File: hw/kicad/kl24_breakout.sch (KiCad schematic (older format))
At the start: 64 parts, among them J1 USB-micro-ab, J2 ARM_10PIN, P1 BATT+, P10 TST, P11 TST, P12 TST, P13 TST, P14 TST, P15 TST, P16 TST, P17 TST, P18 TST, P19 TST, P2 BATT-, P20 TST, P21 TST, P22 TST, P23 TST, P24 TST, P25 TST, P26 TST, P27 TST, P28 TST, P29 TST, P3 BATT_BACKUP+, P30 TST, P31 TST, P32 TST, P33 TST, P34 TST, P35 TST, P36 TST, P4 BATT_BACKUP-, P5 TST, P6 TST, P7 TST, P8 TST, P9 TST, U1 MCP1252-33X50I, U2 MCP73831, U3 MKL24Z64VFM4, U4 MCP1640_SOT23, U5 LP3985, X1 CRYSTAL

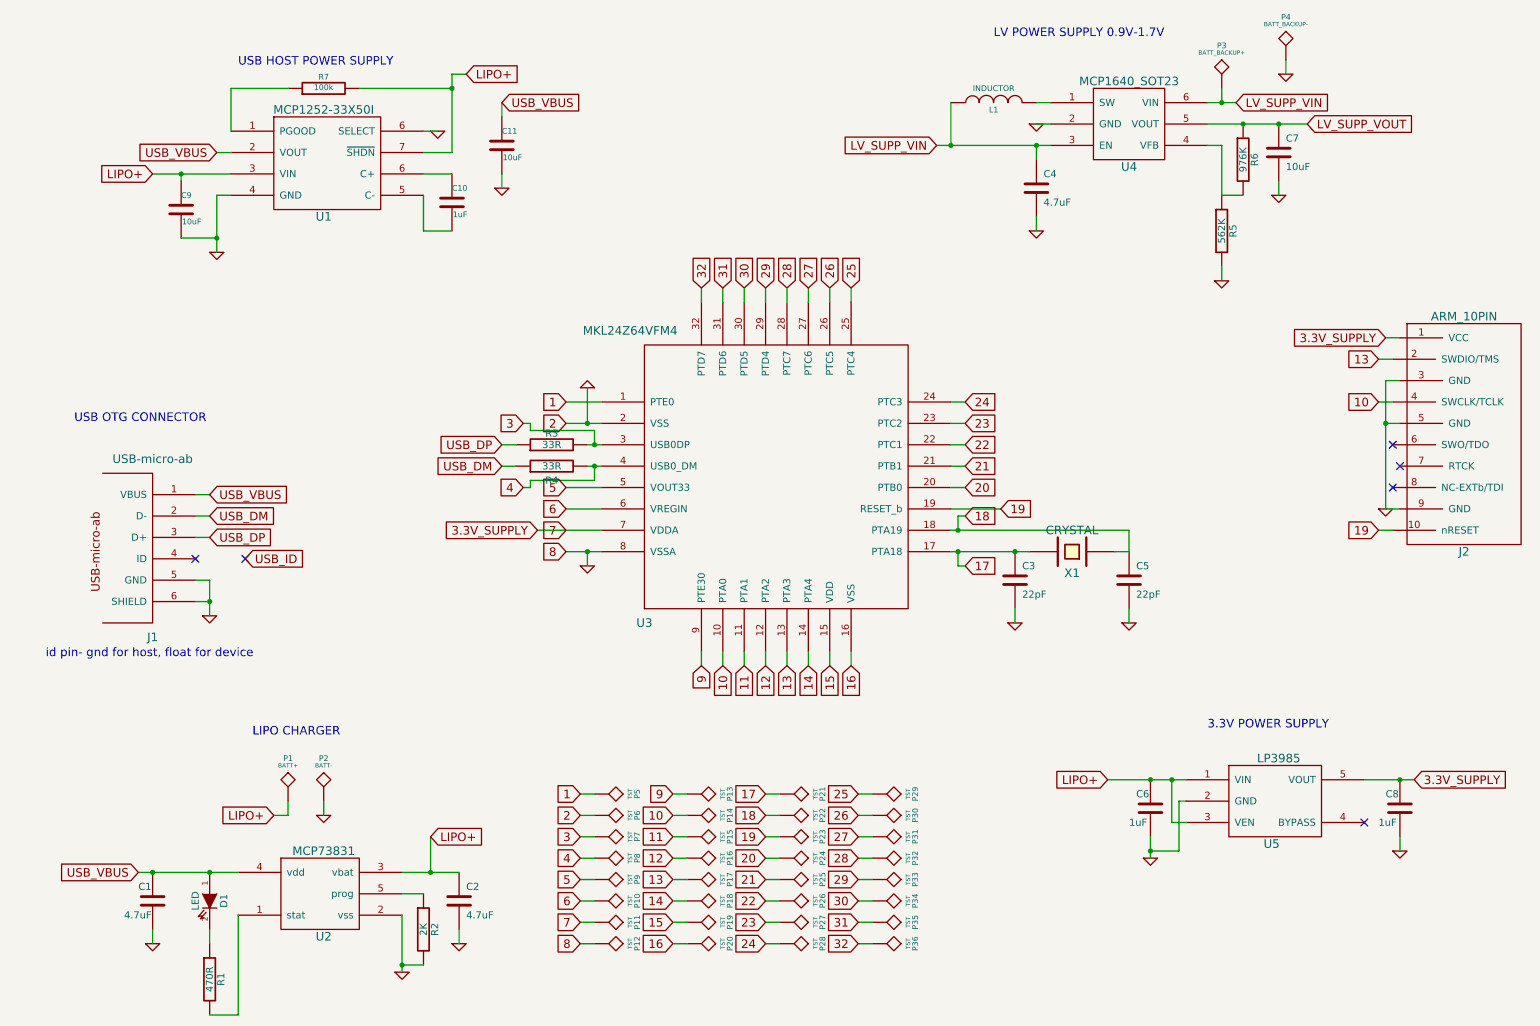
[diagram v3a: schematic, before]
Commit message: - add spi flash
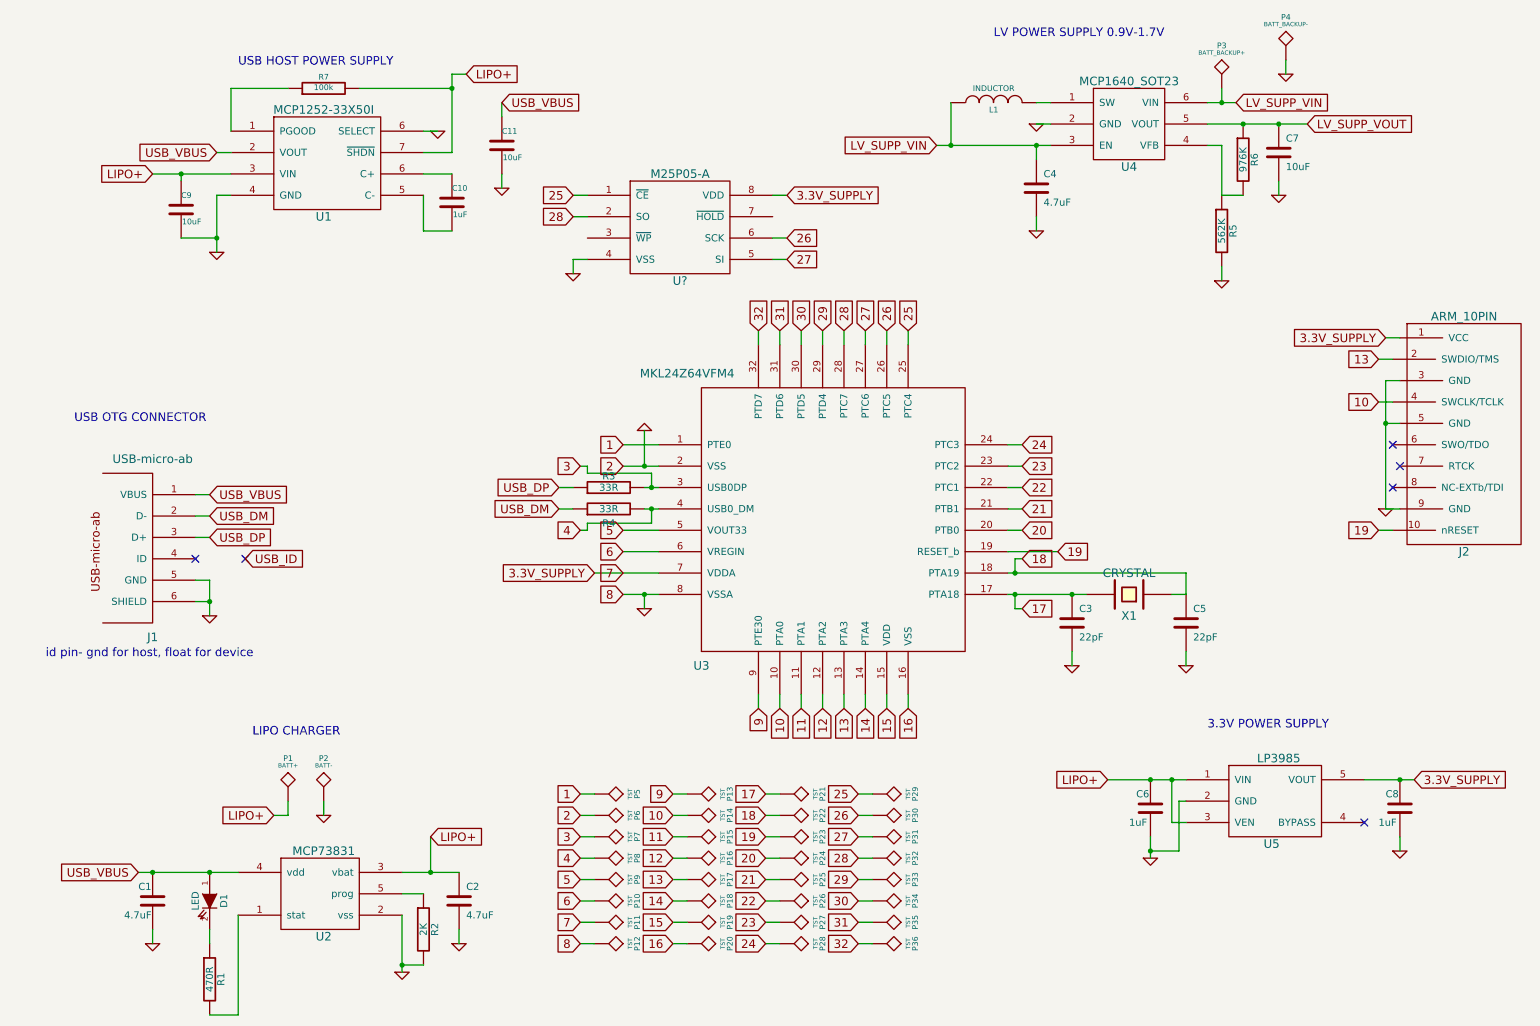
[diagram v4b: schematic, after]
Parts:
- added U?: M25P05-A, symbol M25P05-A
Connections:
- net 25: now also U?.1 (~CE)
- net 26: now also U?.6 (SCK)
- net 27: now also U?.5 (SI)
- net 28: now also U?.2 (SO)
- net 3.3V_SUPPLY: now also U?.8 (VDD)
- net GND: now also U?.4 (VSS)
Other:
- moved on the sheet: C3, C5, R3, R4, U3, X1

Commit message: - create netlist
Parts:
- gave numbers to parts that had none: 1
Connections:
- no-connect marks 6 -> 8
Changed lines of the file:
@@
-EESchema Schematic File Version 2  date 3/21/2013 8:03:57 PM
+EESchema Schematic File Version 2  date 3/21/2013 8:10:15 PM
 LIBS:power
 LIBS:device
@@
 $EndDescr
 $Comp
-L GND #PWR7
+L GND #PWR01
 U 1 1 513B71D5
 P 3500 7050
-F 0 "#PWR7" H 3500 7050 30  0001 C CNN
+F 0 "#PWR01" H 3500 7050 30  0001 C CNN
 F 1 "GND" H 3500 6980 30  0001 C CNN
 F 2 "" H 3500 7050 60  0001 C CNN
@@
 $EndComp
 $Comp
-L GND #PWR1
+L GND #PWR02
 U 1 1 513B7111
 P 1350 7050
-F 0 "#PWR1" H 1350 7050 30  0001 C CNN
+F 0 "#PWR02" H 1350 7050 30  0001 C CNN
 F 1 "GND" H 1350 6980 30  0001 C CNN
 F 2 "" H 1350 7050 60  0001 C CNN
@@
 USB_VBUS
 $Comp
-L GND #PWR5
+L GND #PWR03
 U 1 1 513B7076
 P 3100 7250
-F 0 "#PWR5" H 3100 7250 30  0001 C CNN
+F 0 "#PWR03" H 3100 7250 30  0001 C CNN
 F 1 "GND" H 3100 7180 30  0001 C CNN
 F 2 "" H 3100 7250 60  0001 C CNN
@@
 $EndComp
 $Comp
-L GND #PWR17
+L GND #PWR04
 U 1 1 513B6CEE
 P 9250 1800
-F 0 "#PWR17" H 9250 1800 30  0001 C CNN
+F 0 "#PWR04" H 9250 1800 30  0001 C CNN
 F 1 "GND" H 9250 1730 30  0001 C CNN
 F 2 "" H 9250 1800 60  0001 C CNN
@@
 $EndComp
 $Comp
-L GND #PWR16
+L GND #PWR05
 U 1 1 513B6C70
 P 8850 2400
-F 0 "#PWR16" H 8850 2400 30  0001 C CNN
+F 0 "#PWR05" H 8850 2400 30  0001 C CNN
 F 1 "GND" H 8850 2330 30  0001 C CNN
 F 2 "" H 8850 2400 60  0001 C CNN
@@
 $EndComp
 $Comp
-L GND #PWR12
+L GND #PWR06
 U 1 1 513B6C39
 P 7550 1300
-F 0 "#PWR12" H 7550 1300 30  0001 C CNN
+F 0 "#PWR06" H 7550 1300 30  0001 C CNN
 F 1 "GND" H 7550 1230 30  0001 C CNN
 F 2 "" H 7550 1300 60  0001 C CNN
@@
 $EndComp
 $Comp
-L GND #PWR13
+L GND #PWR07
 U 1 1 513B6C33
 P 7550 2050
-F 0 "#PWR13" H 7550 2050 30  0001 C CNN
+F 0 "#PWR07" H 7550 2050 30  0001 C CNN
 F 1 "GND" H 7550 1980 30  0001 C CNN
 F 2 "" H 7550 2050 60  0001 C CNN
@@
 LV_SUPP_VIN
 $Comp
-L GND #PWR2
+L GND #PWR08
 U 1 1 513B6B06
 P 1750 4750
-F 0 "#PWR2" H 1750 4750 30  0001 C CNN
+F 0 "#PWR08" H 1750 4750 30  0001 C CNN
 F 1 "GND" H 1750 4680 30  0001 C CNN
 F 2 "" H 1750 4750 60  0001 C CNN
@@
 $EndComp
 $Comp
-L GND #PWR4
+L GND #PWR09
 U 1 1 513B6AFE
 P 2550 6150
-F 0 "#PWR4" H 2550 6150 30  0001 C CNN
+F 0 "#PWR09" H 2550 6150 30  0001 C CNN
 F 1 "GND" H 2550 6080 30  0001 C CNN
 F 2 "" H 2550 6150 60  0001 C CNN
@@
 $EndComp
 $Comp
-L GND #PWR18
+L GND #PWR010
 U 1 1 513B6A86
 P 9300 950
-F 0 "#PWR18" H 9300 950 30  0001 C CNN
+F 0 "#PWR010" H 9300 950 30  0001 C CNN
 F 1 "GND" H 9300 880 30  0001 C CNN
 F 2 "" H 9300 950 60  0001 C CNN
@@
 $EndComp
 $Comp
-L GND #PWR11
+L GND #PWR011
 U 1 1 513BAD17
 P 7800 5100
-F 0 "#PWR11" H 7800 5100 30  0001 C CNN
+F 0 "#PWR011" H 7800 5100 30  0001 C CNN
 F 1 "GND" H 7800 5030 30  0001 C CNN
 F 2 "" H 7800 5100 60  0001 C CNN
@@
 $EndComp
 $Comp
-L GND #PWR14
+L GND #PWR012
 U 1 1 513BAD27
 P 8600 5100
-F 0 "#PWR14" H 8600 5100 30  0001 C CNN
+F 0 "#PWR012" H 8600 5100 30  0001 C CNN
 F 1 "GND" H 8600 5030 30  0001 C CNN
 F 2 "" H 8600 5100 60  0001 C CNN
@@
 19
 $Comp
-L GND #PWR19
+L GND #PWR013
 U 1 1 513F9714
 P 10000 4000
-F 0 "#PWR19" H 10000 4000 30  0001 C CNN
+F 0 "#PWR013" H 10000 4000 30  0001 C CNN
 F 1 "GND" H 10000 3930 30  0001 C CNN
 F 2 "" H 10000 4000 60  0001 C CNN
@@
 LIPO+
 $Comp
-L GND #PWR15
+L GND #PWR014
 U 1 1 513F9B6C
 P 8350 6450
-F 0 "#PWR15" H 8350 6450 30  0001 C CNN
+F 0 "#PWR014" H 8350 6450 30  0001 C CNN
 F 1 "GND" H 8350 6380 30  0001 C CNN
 F 2 "" H 8350 6450 60  0001 C CNN
@@
 $EndComp
 $Comp
-L GND #PWR20
+L GND #PWR015
 U 1 1 513F9C7F
 P 10100 6400
-F 0 "#PWR20" H 10100 6400 30  0001 C CNN
+F 0 "#PWR015" H 10100 6400 30  0001 C CNN
 F 1 "GND" H 10100 6330 30  0001 C CNN
 F 2 "" H 10100 6400 60  0001 C CNN
@@
 3.3V_SUPPLY
 $Comp
-L GND #PWR10
+L GND #PWR016
 U 1 1 513FA04E
 P 4800 4700
-F 0 "#PWR10" H 4800 4700 30  0001 C CNN
+F 0 "#PWR016" H 4800 4700 30  0001 C CNN
 F 1 "GND" H 4800 4630 30  0001 C CNN
 F 2 "" H 4800 4700 60  0001 C CNN
@@
 $EndComp
 $Comp
-L GND #PWR9
+L GND #PWR017
 U 1 1 513FA1BA
 P 4800 3450
-F 0 "#PWR9" H 4800 3450 30  0001 C CNN
+F 0 "#PWR017" H 4800 3450 30  0001 C CNN
 F 1 "GND" H 4800 3380 30  0001 C CNN
 F 2 "" H 4800 3450 60  0001 C CNN
@@
 3.3V_SUPPLY
 $Comp
-L GND #PWR3
+L GND #PWR018
 U 1 1 513FAD8F
 P 1800 2200
-F 0 "#PWR3" H 1800 2200 30  0001 C CNN
+F 0 "#PWR018" H 1800 2200 30  0001 C CNN
 F 1 "GND" H 1800 2130 30  0001 C CNN
 F 2 "" H 1800 2200 60  0001 C CNN
@@
 $EndComp
 $Comp
-L GND #PWR6
+L GND #PWR019
 U 1 1 514A1A73
 P 3350 1350
-F 0 "#PWR6" H 3350 1350 30  0001 C CNN
+F 0 "#PWR019" H 3350 1350 30  0001 C CNN
 F 1 "GND" H 3350 1280 30  0001 C CNN
 F 2 "" H 3350 1350 60  0001 C CNN
@@
 USB_VBUS
 $Comp
-L GND #PWR8
+L GND #PWR020
 U 1 1 514A1C2B
 P 3800 1750
-F 0 "#PWR8" H 3800 1750 30  0001 C CNN
+F 0 "#PWR020" H 3800 1750 30  0001 C CNN
 F 1 "GND" H 3800 1680 30  0001 C CNN
 F 2 "" H 3800 1750 60  0001 C CNN
@@
 NoConn ~ 2000 4350
 $Comp
-L M25P05-A U?
+L M25P05-A U6
 U 1 1 514BA0D4
 P 5050 2000
-F 0 "U?" H 5050 1600 60  0000 C CNN
+F 0 "U6" H 5050 1600 60  0000 C CNN
 F 1 "M25P05-A" H 5050 2350 60  0000 C CNN
 F 2 "" H 5100 1800 60  0000 C CNN
@@
 	4300 1800 4400 1800
 $Comp
-L GND #PWR?
+L GND #PWR021
 U 1 1 514BA584
 P 4300 2350
-F 0 "#PWR?" H 4300 2350 30  0001 C CNN
+F 0 "#PWR021" H 4300 2350 30  0001 C CNN
 F 1 "GND" H 4300 2280 30  0001 C CNN
 F 2 "" H 4300 2350 60  0001 C CNN
@@
 Wire Wire Line
 	4300 2250 4400 2250
+NoConn ~ 5700 1950
+NoConn ~ 4400 2100
 $EndSCHEMATC

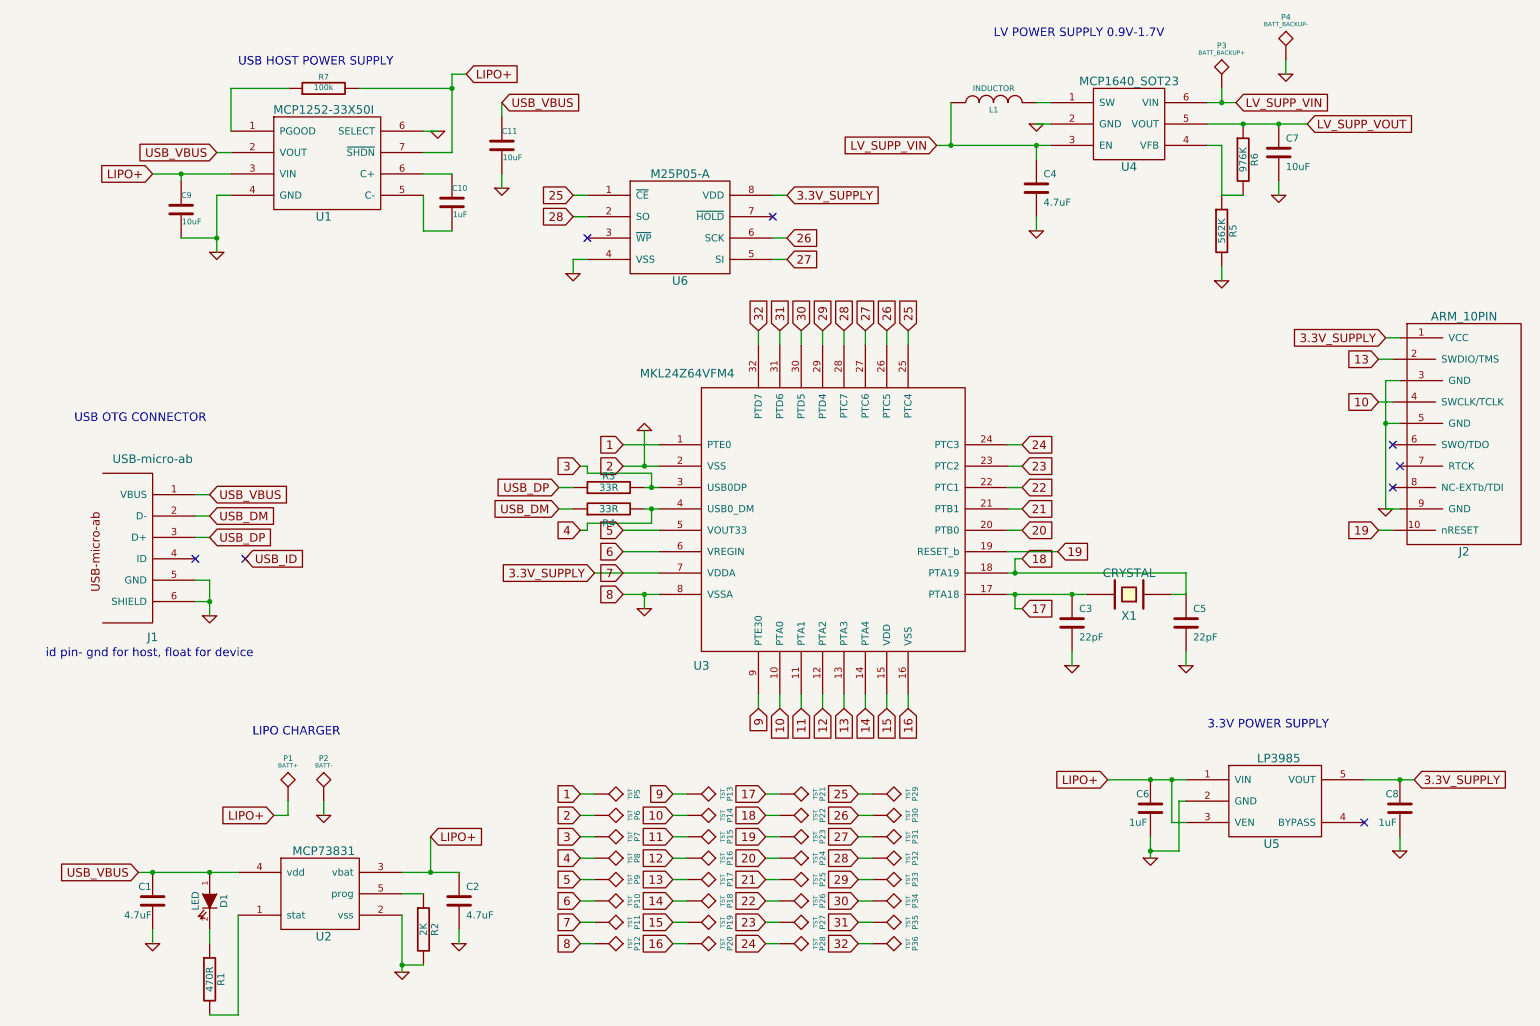
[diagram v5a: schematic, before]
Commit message: - try to rework usb host pwr supply, needs an extra switch i'm thinking, so i'm bailing
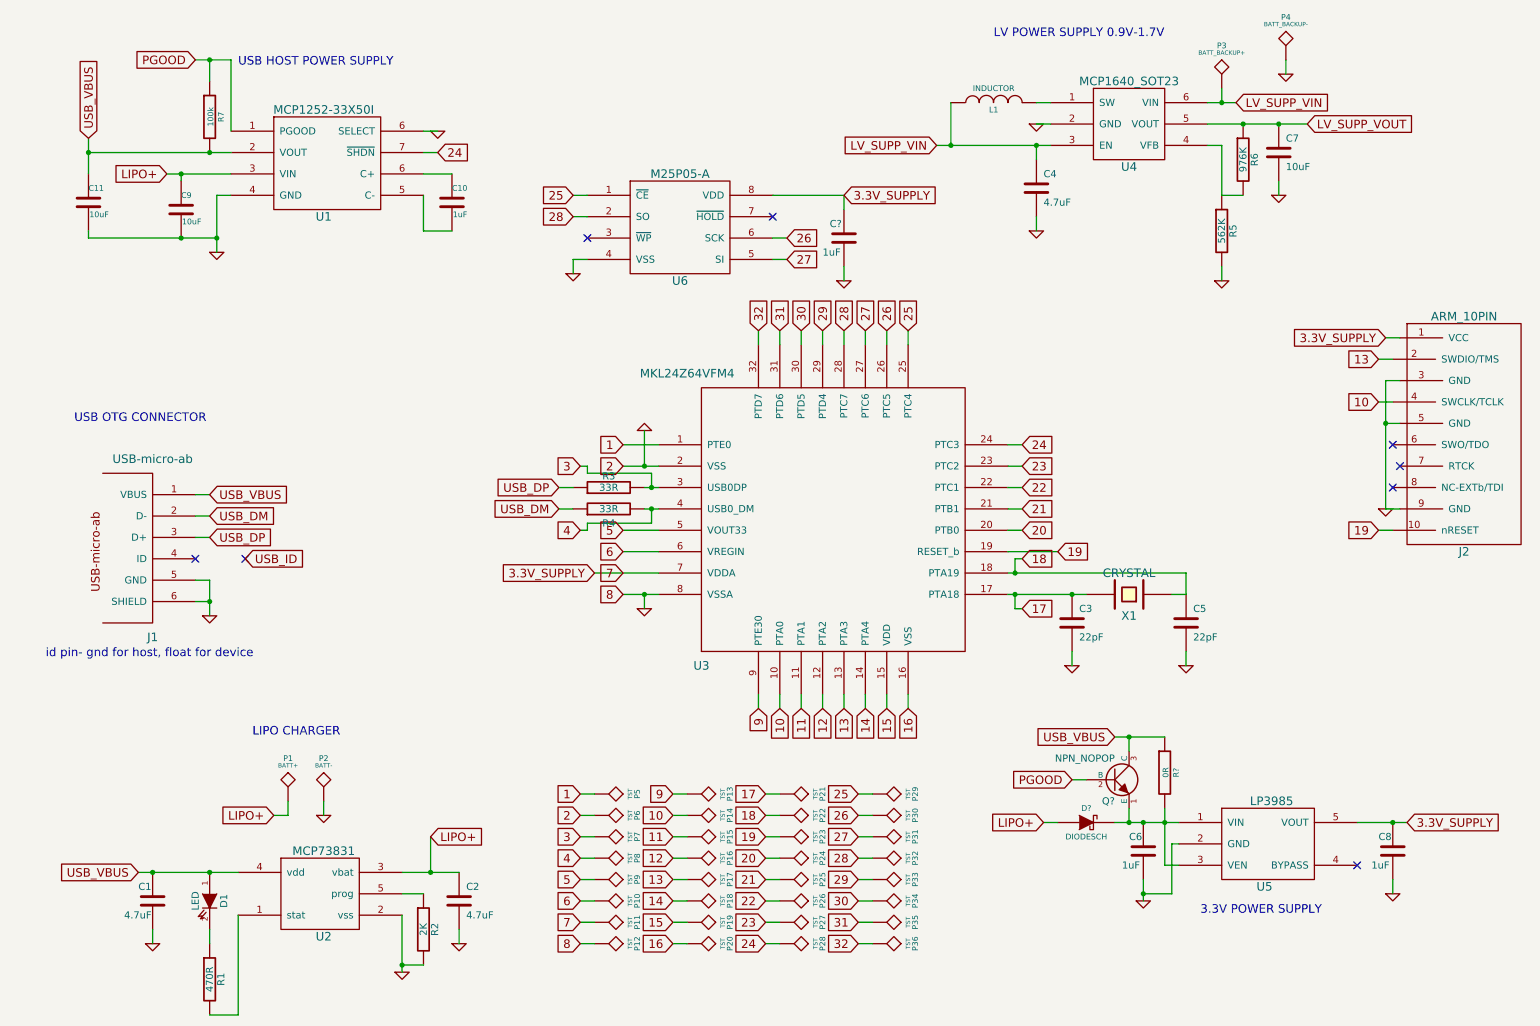
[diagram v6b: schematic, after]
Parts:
- added C?: 1uF, symbol C
- added D?: DIODESCH, ~, symbol DIODESCH
- added Q?: NPN_NOPOP, ~, symbol NPN
- added R?: 0R, ~, symbol R
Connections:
- net 24: now also U1.7 (~SHDN)
- net 3.3V_SUPPLY: now also C?.1
- net GND: now also C?.2
- net LIPO+: now also D?.1 (A); no longer C6.1, R7.2, U1.7 (~SHDN), U5.1 (VIN), U5.3 (VEN)
- net USB_VBUS: now also R7.2, Q?.3 (C), R?.1
- net PGOOD: now reaches R7.1, U1.1 (PGOOD)
- net PGOOD: now also Q?.2 (B)
- new net: C6.1, D?.2 (K), Q?.1 (E), R?.2, U5.1 (VIN), U5.3 (VEN)
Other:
- moved on the sheet: C11, C6, C8, R7, U5
